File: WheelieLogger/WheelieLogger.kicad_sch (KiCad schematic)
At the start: 31 parts, among them J1 USB_C_Plug_USB2.0, J2 Conn_Power, SW1 SW_RESET, U1 GD25Q32CNIGR, U2 MCP1700-3302E_SOT23, U3 ATSAMD21E18A, U4 MPU-6050

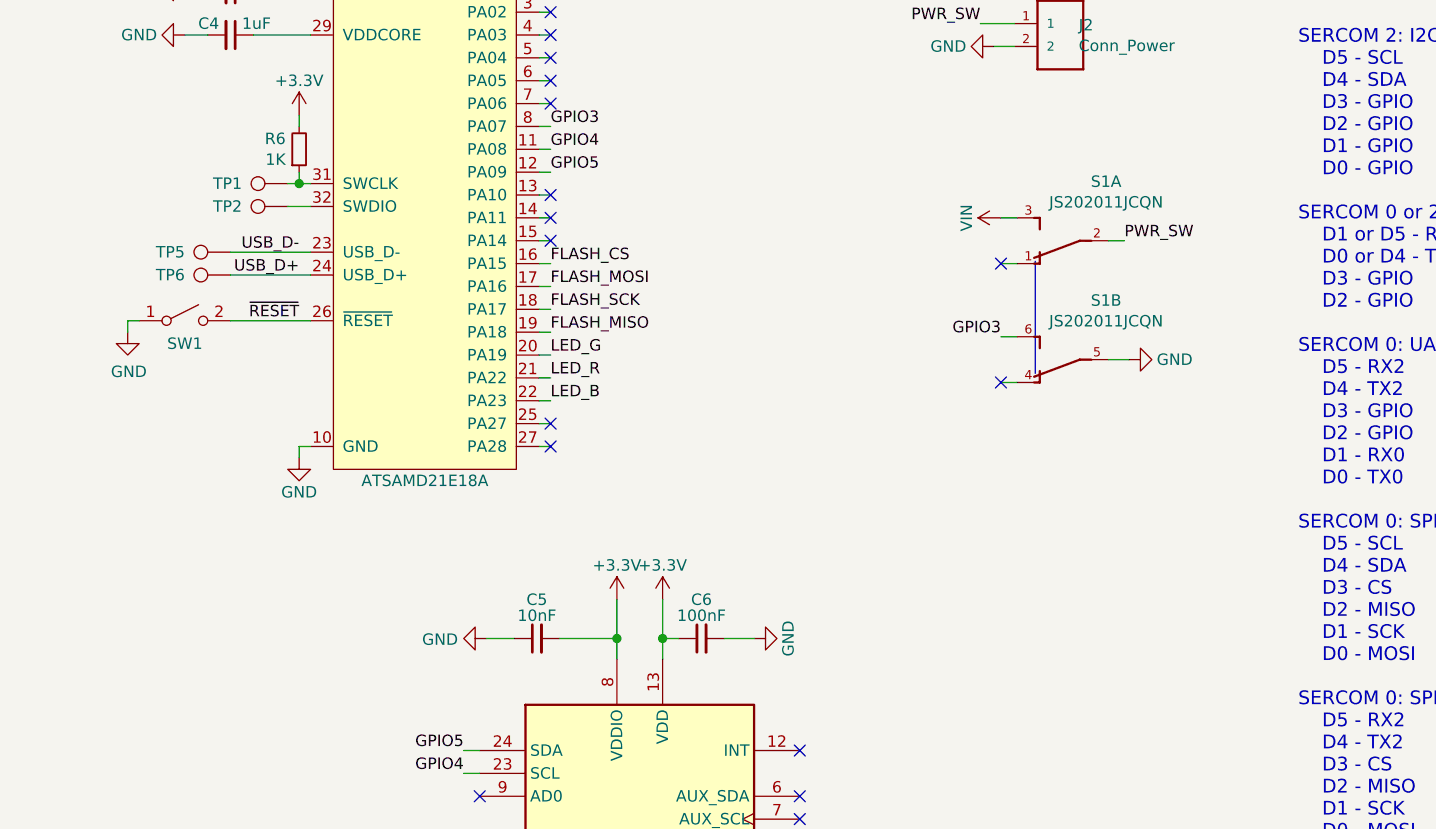
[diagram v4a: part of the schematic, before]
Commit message: Added J-link connector Moved the diodes to make room for it
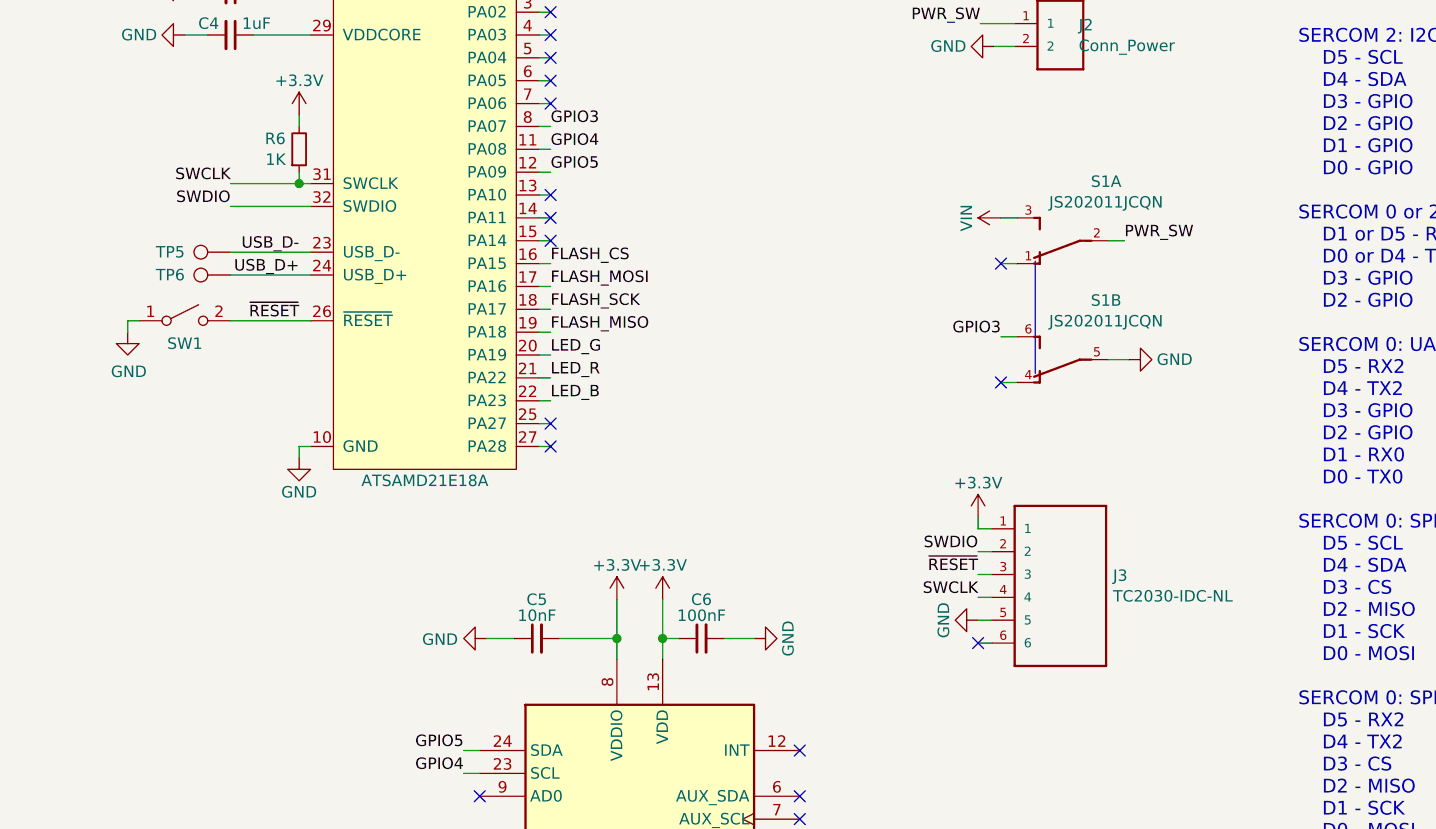
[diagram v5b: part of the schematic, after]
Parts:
- removed TP1: TP_SWCLK, TestPoint:TestPoint_Pad_D1.0mm, symbol Connector:TestPoint
- removed TP2: TP_SWDIO, TestPoint:TestPoint_Pad_D1.0mm, symbol Connector:TestPoint
- added J3: TC2030-IDC-NL, TAG_TC2030-IDC-NL, symbol TC2030-IDC-NL:TC2030-IDC-NL
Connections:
- net +3V3: now also J3.1
- net GND: now also J3.5
- net ~RESET~: now also J3.3
- net SWCLK: now reaches R6.1, U3.31 (SWCLK)
- net SWCLK: now also J3.4
- net SWDIO: now reaches U3.32 (SWDIO)
- net SWDIO: now also J3.2
- no-connect marks 21 -> 22

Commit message: Updated to version 2
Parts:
- removed unit 1 of S1
- added C10, C11: 1uF, Capacitor_SMD:C_0402_1005Metric, symbol Device:C_Small
- added D4: Red, LED_SMD:LED_0402_1005Metric, symbol Device:LED_Small
- added D5: Yellow, LED_SMD:LED_0402_1005Metric, symbol Device:LED_Small
- added D6: Green, LED_SMD:LED_0402_1005Metric, symbol Device:LED_Small
- added R10, R8, R9: 1.5kR, Resistor_SMD:R_0402_1005Metric, symbol Device:R_Small
- added U5: MCP73833-AMI_UN, Footprints:SON50P300X300X100-11N, symbol MCP73833-AMI_UN:MCP73833-AMI_UN
- J3: footprint TAG_TC2030-IDC-NL -> Footprints:Tag-Connect_TC2030-IDC-NL
- S1: footprint Button_Switch_THT:SW_CuK_JS202011CQN_DPDT_Straight -> Footprints:SW_JS202011JCQN
- U4: LCSC C24112 -> (none)
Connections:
- net +3V3: now also C9.2, U2.2 (VO); no longer C9.1
- net +5V: now also C10.1, D4.2 (A), D5.2 (A), D6.2 (A), U5.1 (VDD), U5.2 (VDD)
- net GND: now also C9.1, S1.2, C10.2, C11.1, U5.5 (VSS); no longer S1.5
- net GPIO3: now also S1.1; no longer S1.6
- net PWR_SW: now also S1.5
- net VIN: now also S1.6, C11.2, U5.10 (VBAT), U5.9 (VBAT)
- new net: R9.1, U5.3 (STAT1)
- new net: D5.1 (K), R9.2
- new net: R10.1, U5.4 (STAT2)
- new net: R8.1, U5.7 (~PG)
- new net: D4.1 (K), R8.2
- new net: D6.1 (K), R10.2
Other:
- note removed: "SERCOM 3 is always SPI FLASH Possible configs: SERCOM 0: SPI D5 - GPIO D4 - GPIO D3 - CS D2 - MISO D1 - SCK D0 - MOSI SERCOM 2: I2C D5 - SCL D4 - SDA D3 - GPIO D2 - GPIO D1 - GPIO D0 - GPIO SERCOM 0 or 2: UART D1 or D5 - RX D0 or D4 - TX D3 - GPIO D2 - GPIO SERCOM 0: UART, SERCOM 2: UART (2x UART) D5 - RX2 D4 - TX2 D3 - GPIO D2 - GPIO D1 - RX0 D0 - TX0 SERCOM 0: SPI, SERCOM 2: I2C D5 - SCL D4 - S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"
- moved on the sheet: C9, J3
